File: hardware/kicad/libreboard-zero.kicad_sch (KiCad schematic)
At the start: 0 parts

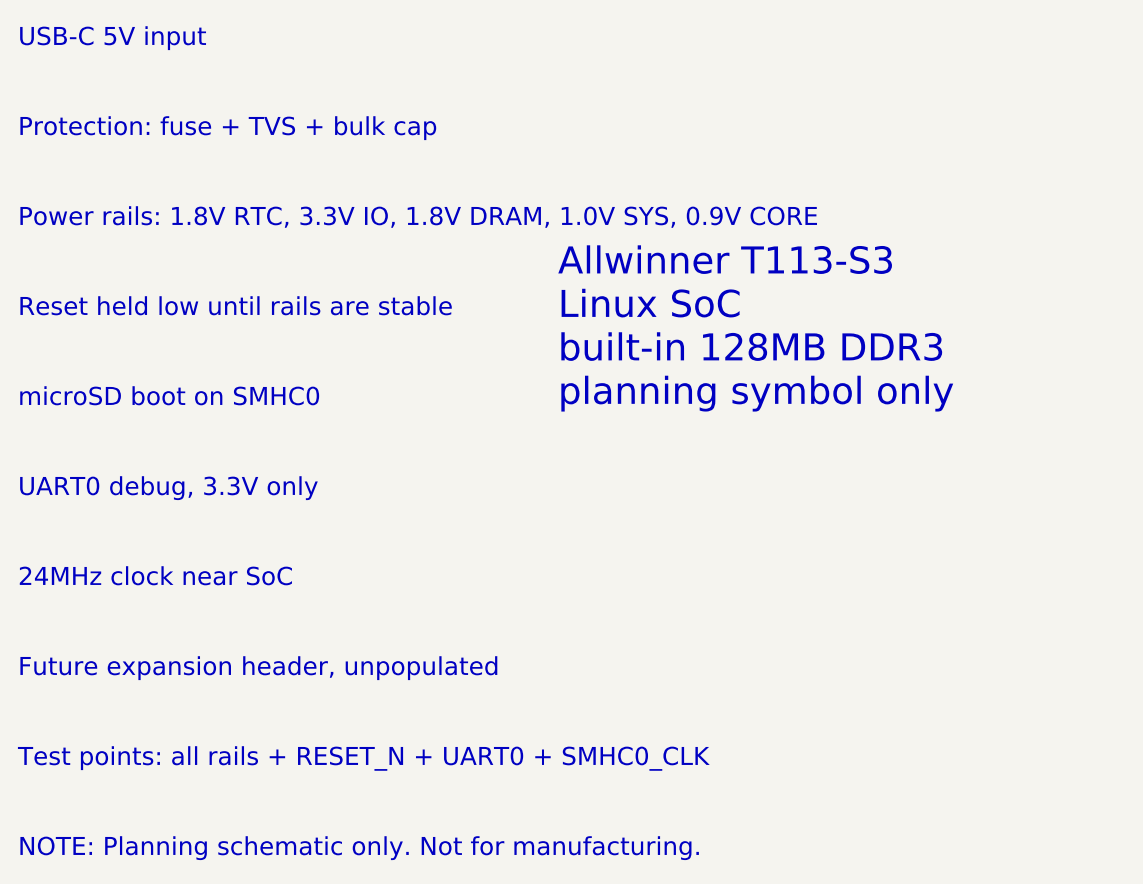
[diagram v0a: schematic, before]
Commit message: Update planning schematic labels for UART3 and DRAM 1.5V
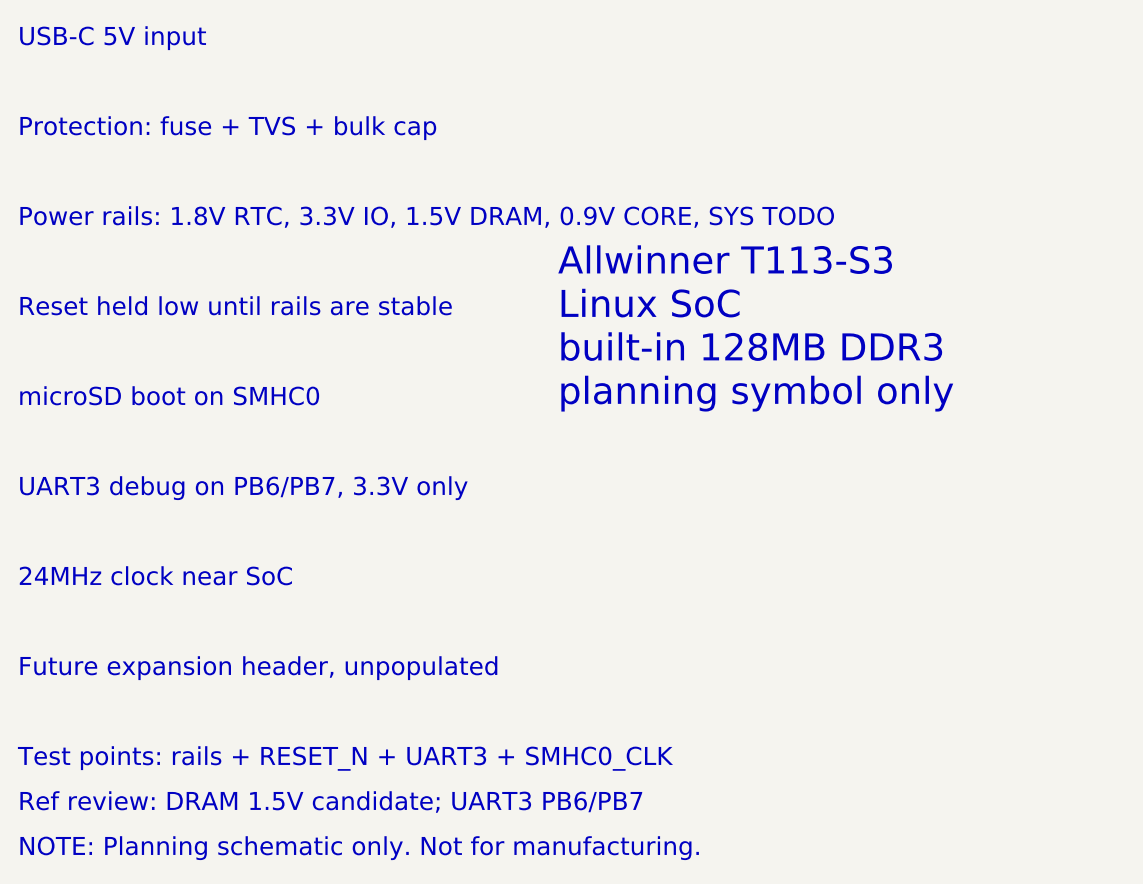
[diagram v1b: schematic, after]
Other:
- note added: "Power rails: 1.8V RTC, 3.3V IO, 1.5V DRAM, 0.9V CORE, SYS TODO"
- note added: "Ref review: DRAM 1.5V candidate; UART3 PB6/PB7"
- note added: "Test points: rails + RESET_N + UART3 + SMHC0_CLK"
- note added: "UART3 debug on PB6/PB7, 3.3V only"
- note removed: "Power rails: 1.8V RTC, 3.3V IO, 1.8V DRAM, 1.0V SYS, 0.9V CORE"
- note removed: "Test points: all rails + RESET_N + UART0 + SMHC0_CLK"
- note removed: "UART0 debug, 3.3V only"
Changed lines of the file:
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@@
 		(comment 2 "https://github.com/zeyadhost/libreboard-zero")
 	)
-	(text "UART0 debug, 3.3V only"
+	(text "UART3 debug on PB6/PB7, 3.3V only"
 		(exclude_from_sim no)
 		(at 40 90 0)
@@
 		)
 	)
-	(text "Power rails: 1.8V RTC, 3.3V IO, 1.8V DRAM, 1.0V SYS, 0.9V CORE"
+	(text "Power rails: 1.8V RTC, 3.3V IO, 1.5V DRAM, 0.9V CORE, SYS TODO"
 		(exclude_from_sim no)
 		(at 40 60 0)
@@
 		)
 	)
-	(text "Test points: all rails + RESET_N + UART0 + SMHC0_CLK"
+	(text "Test points: rails + RESET_N + UART3 + SMHC0_CLK"
 		(exclude_from_sim no)
 		(at 40 120 0)
@@
 			)
 			(justify left bottom)
+		)
+	)
+	(text "Ref review: DRAM 1.5V candidate; UART3 PB6/PB7"
+		(exclude_from_sim no)
+		(at 40 125 0)
+		(effects
+			(font
+				(size 2 2)
+			)
+			(justify left bottom)
